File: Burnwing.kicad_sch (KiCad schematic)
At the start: 57 parts, among them J1 Conn_01x04_Socket, J2 USB Type C, J3 Conn_01x02_Pin, J4 Conn_01x02_Pin, J5 Conn_01x06_MountingPin, J6 Conn_01x06_MountingPin, Q1 AONR21307, SW1 SW_DIP_x02, U1 HUSB238, U2 BTS7030-2EPA, U3 TPS70933QDBVRQ1

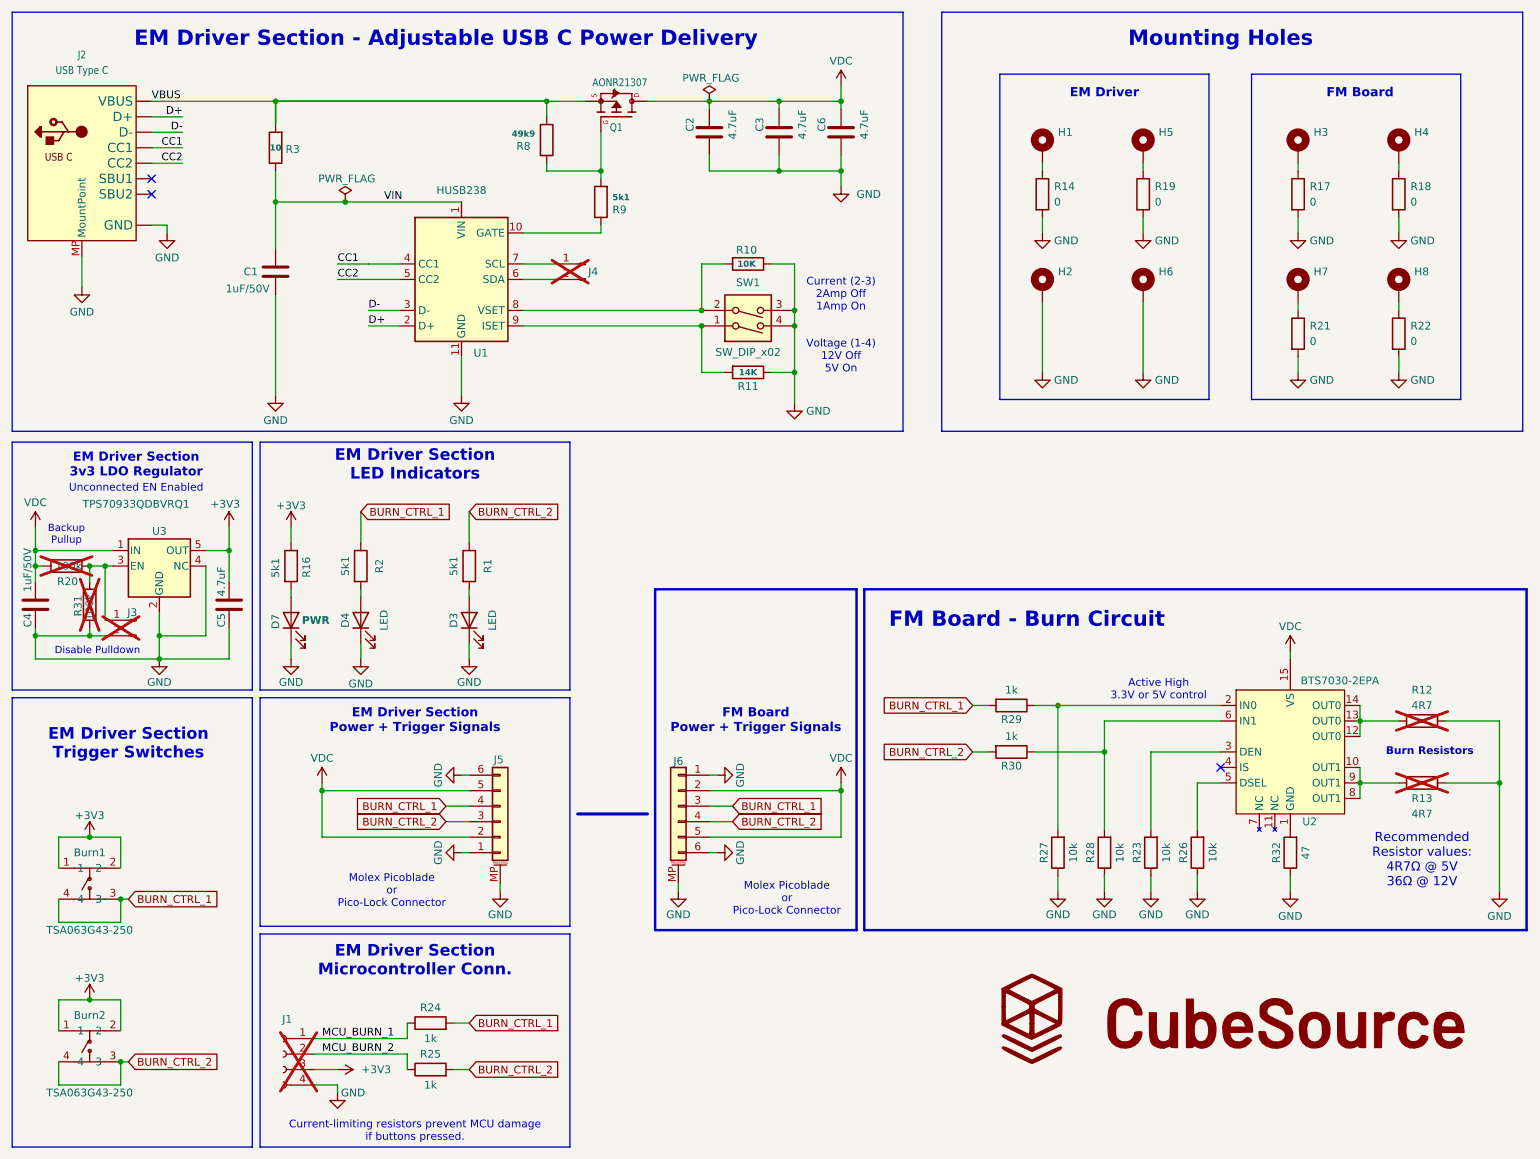
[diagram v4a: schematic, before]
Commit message: Apply design review fixes, clean up BOM and footprint library
Board now passes DRC with 0 violations, 0 unconnected items and 0 schematic
parity errors. ERC is down to one pre-existing power_pin_not_driven on U2 pin 1.

Component values (from the design review):
- R29, R30: 1k -> 3k on the control-line series resistance. At 12 V into a
  3.3 V host this is 25 mW against a 50 mW derated budget; 1k gave 76 mW and
  failed the 50% derate. 3k + the 1k on the J1 path stays under the 4.7k the
  driver datasheet recommends
- R1, R2, R16: 5k1 -> 150R on the LED series resistors. 5k1 gave ~0.25 mA and
  was effectively invisible. 150R gives 8.7 mA at 3.3 V and stays safe at 20 mA
  if a control line is driven at 5 V
- R20, R31: 100k -> 10k on the LDO EN divider pads (both DNP). 100k is high
  enough to affect the LDO's turn-on and settling behaviour if ever populated

Connectivity:
- Wire Burn2 pin 1 to +3V3. Burn1 had both pads 1 and 2 on the net but Burn2
  had only pad 2, leaving pad 1 on no net at all
- Add jumper pad groups (1+2, 3+4) to the tact switch footprint, declaring the
  internally bonded pads so DRC no longer reports them as unconnected. This
  resolved the remaining teardrop unconnected items

BOM correctness:
- C105580 is a 5.1k part but was assigned to five components across three
  values. R9 keeps it; R1/R2/R16 -> C22808 (150R), R11 -> C881028 (14k)
- Burn1, Burn2 and U2 stored their code in a field named "LCSC Part" rather
  than "LCSC", so a BOM export keyed on LCSC silently dropped them, including
  the driver IC
- Add missing codes: R29/R30 -> C881244, R17/R18/R19/R21/R22 -> C100044,
  matching R14

Footprint library:
- Add MountingHole_2.2mm_M2_Pad_4mm and reassign H2/H6 to it. Those two sit
  closest to the panel break line and use a 4.0 mm pad against 4.4 mm on the
  other six; a shared footprint could not represent both
- CONN-SMD_6P-P1.50_A1501WRB-S-6P: convert from the legacy (module format left
  by the EasyEDA importer, which also carried an e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
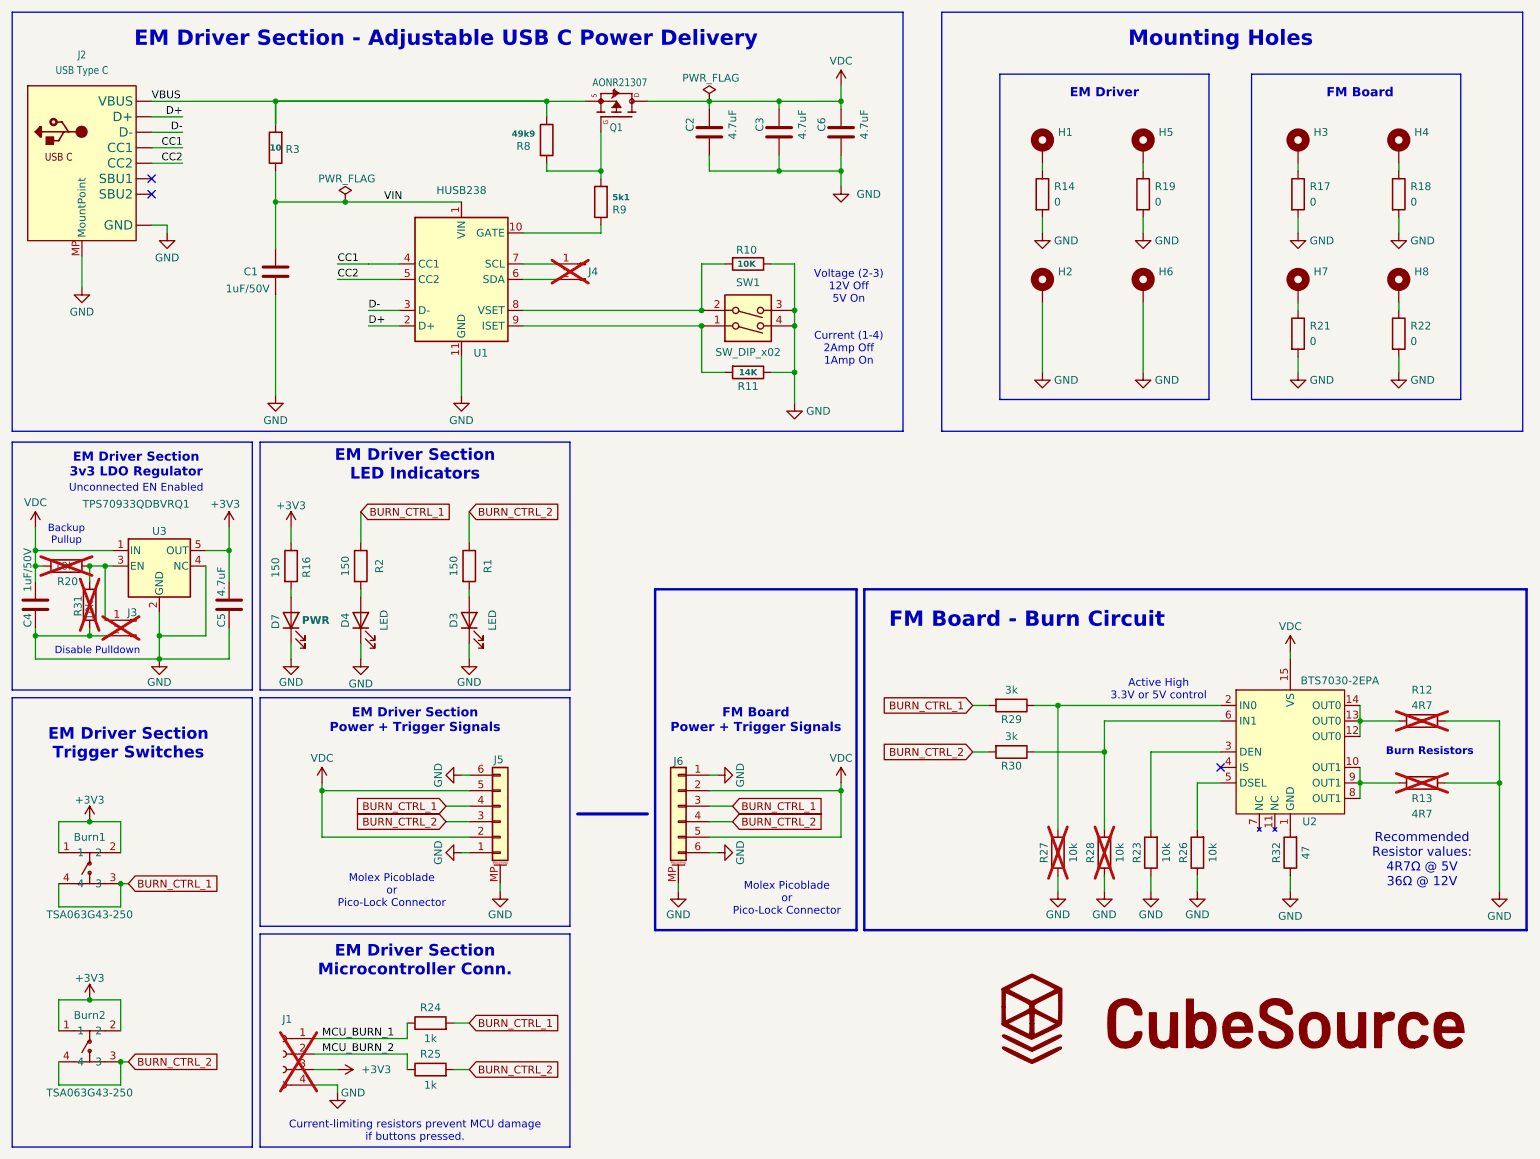
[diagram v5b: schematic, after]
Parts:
- Burn1: symbol Burnwing:TSA063G43-250 -> Burnwing:TSA063G43-250_1; LCSC (none) -> C294564
- Burn2: LCSC (none) -> C294564
- H2, H6: footprint Burnwing:MountingHole_2.2mm_M2_Pad -> Burnwing:MountingHole_2.2mm_M2_Pad_4mm
- J5: footprint Burnwing:Molex_Pico-Lock_and_PicoBlade -> Burnwing:Molex_Pico-Lock_and_PicoBlade_Mirror
- R1, R16, R2: value 5k1 -> 150; LCSC C105580 -> C22808
- R11: LCSC C105580 -> C881028
- R17, R18, R19, R21, R22: LCSC (none) -> C100044
- R20, R31: value 100k -> 10k
- R27, R28: now not fitted; now left out of the parts list
- R29, R30: value 1k -> 3k; LCSC (none) -> C881244
- U2: LCSC (none) -> C534836
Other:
- note added: "Current (1-4) 2Amp Off 1Amp On"
- note added: "Voltage (2-3) 12V Off 5V On"
- note removed: "Current (2-3) 2Amp Off 1Amp On"
- note removed: "Voltage (1-4) 12V Off 5V On"
- moved on the sheet: Burn1

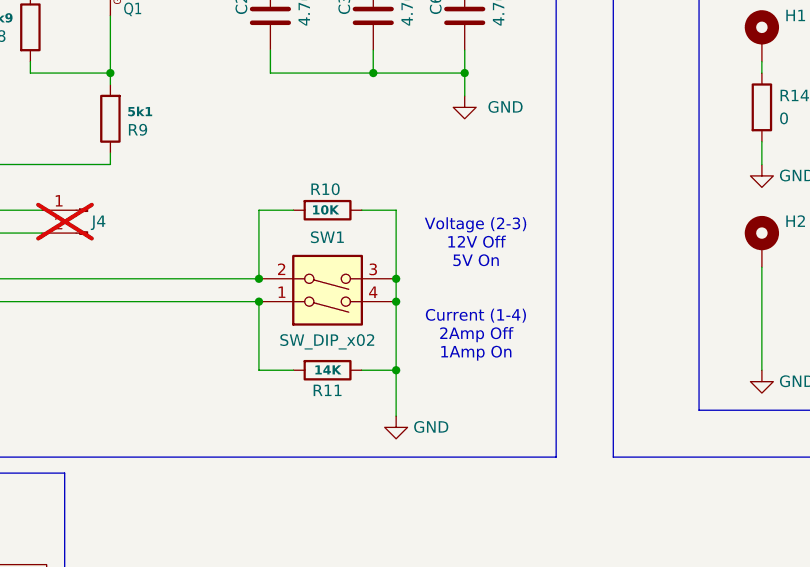
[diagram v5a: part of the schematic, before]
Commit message: Correct SW1 pole assignment so legends match function
The DIP switch poles drove the opposite functions to their printed legends:
the pole marked for voltage switched ISET, and the pole marked for current
switched VSET.

Swap the pole assignments so each matches its legend:
- SW1 pin 1 (switch 1, pins 1-4) now drives VSET
- SW1 pin 2 (switch 2, pins 2-3) now drives ISET

Schematic annotation updated to match: "Voltage (1-4)" and "Current (2-3)",
previously "(2-3)" and "(1-4)" respectively.

Resistor values are unchanged and were always correct - R10 = 10k on VSET
requests 12 V open / 5 V closed, R11 = 14k on ISET requests 2.25 A open /
1.25 A closed. Only the mapping of function to physical actuator changed, so
PD behaviour for a correctly-set switch is identical.

DRC: 0 violations, 0 unconnected, 0 schematic parity errors.
ERC: 1 pre-existing power_pin_not_driven on U2 pin 1.
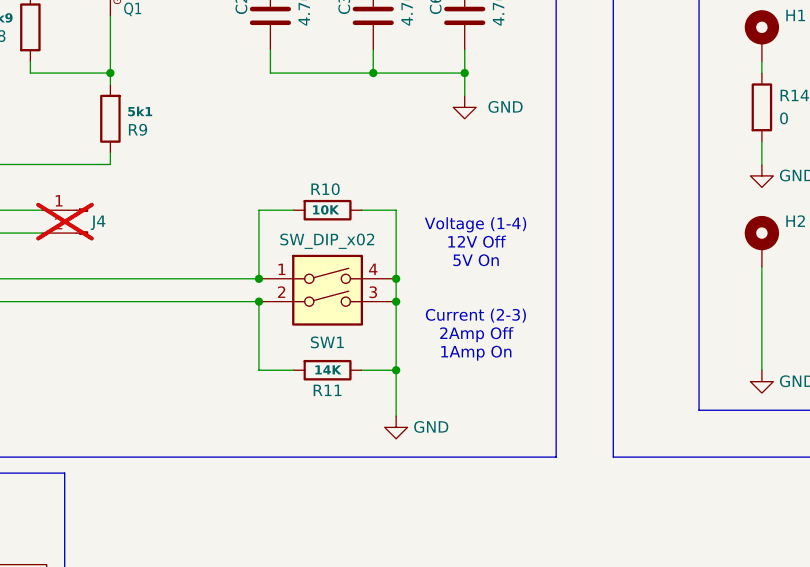
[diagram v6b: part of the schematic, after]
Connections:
- net at R11.2, U1.9 (ISET): now also SW1.2; no longer SW1.1
- net at R10.2, U1.8 (VSET): now also SW1.1; no longer SW1.2
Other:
- note added: "Current (2-3) 2Amp Off 1Amp On"
- note added: "Voltage (1-4) 12V Off 5V On"
- note removed: "Current (1-4) 2Amp Off 1Amp On"
- note removed: "Voltage (2-3) 12V Off 5V On"
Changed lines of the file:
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@@
 		)
 	)
-	(text "Voltage (2-3)\n12V Off\n5V On"
+	(text "Voltage (1-4)\n12V Off\n5V On"
 		(exclude_from_sim no)
 		(at 151.13 59.69 0)
@@
 		)
 	)
-	(text "Current (1-4)\n2Amp Off\n1Amp On"
+	(text "Current (2-3)\n2Amp Off\n1Amp On"
 		(exclude_from_sim no)
 		(at 151.13 69.85 0)
@@
 	)
 	(junction
-		(at 142.24 66.04)
+		(at 127 63.5)
 		(diameter 0)
 		(color 0 0 0 0)
@@
 	)
 	(junction
+		(at 142.24 66.04)
+		(diameter 0)
+		(color 0 0 0 0)
+	)
+	(junction
 		(at 17.78 105.41)
 		(diameter 0)
@@
 	)
 	(junction
+		(at 127 66.04)
+		(diameter 0)
+		(color 0 0 0 0)
+	)
+	(junction
 		(at 26.67 176.53)
 		(diameter 0)
@@
 	)
 	(junction
+		(at 142.24 63.5)
+		(diameter 0)
+		(color 0 0 0 0)
+	)
+	(junction
 		(at 142.24 73.66)
 		(diameter 0)
@@
 	)
 	(junction
-		(at 127 66.04)
-		(diameter 0)
-		(color 0 0 0 0)
-	)
-	(junction
 		(at 17.78 102.87)
 		(diameter 0)
@@
 	)
 	(junction
-		(at 142.24 63.5)
-		(diameter 0)
-		(color 0 0 0 0)
-	)
-	(junction
 		(at 31.75 186.69)
 		(diameter 0)
@@
 	)
 	(junction
-		(at 127 63.5)
-		(diameter 0)
-		(color 0 0 0 0)
-	)
-	(junction
 		(at 68.58 45.72)
 		(diameter 0)
@@
 	(wire
 		(pts
+			(xy 142.24 66.04) (xy 142.24 73.66)
+		)
+		(stroke
+			(width 0)
+			(type default)
+		)
+	)
+	(wire
+		(pts
 			(xy 138.43 55.88) (xy 142.24 55.88)
 		)
@@
 	(wire
 		(pts
-			(xy 57.15 29.21) (xy 101.6 29.21)
+			(xy 142.24 63.5) (xy 142.24 66.04)
 		)
 		(stroke
@@
 	(wire
 		(pts
-			(xy 142.24 63.5) (xy 142.24 66.04)
+			(xy 57.15 29.21) (xy 101.6 29.21)
 		)
 		(stroke
@@
 	(wire
 		(pts
-			(xy 142.24 66.04) (xy 142.24 73.66)
-		)
-		(stroke
-			(width 0)
-			(type default)
-		)
-	)
-	(wire
-		(pts
 			(xy 101.6 29.21) (xy 107.95 29.21)
 		)
@@
 	(symbol
 		(lib_id "Burnwing:SW_DIP_x02")
-		(at 134.62 63.5 0)
-		(mirror x)
+		(at 134.62 66.04 0)
 		(unit 1)
 		(body_style 1)
@@
 		(dnp no)
 		(property "Reference" "SW1"
-			(at 134.62 58.928 0)
+			(at 134.62 70.612 0)
 			(show_name no)
 			(do_not_autoplace no)
@@
 		)
 		(property "Value" "SW_DIP_x02"
-			(at 134.62 70.358 0)
+			(at 134.62 59.182 0)
 			(show_name no)
 			(do_not_autoplace no)
@@
 		)
 		(property "Footprint" "Burnwing:2_Dipswitch"
-			(at 134.62 63.5 0)
+			(at 134.62 66.04 0)
 			(hide yes)
 			(show_name no)
@@
 		)
 		(property "Datasheet" ""
-			(at 134.62 63.5 0)
+			(at 134.62 66.04 0)
 			(hide yes)
 			(show_name no)
@@
 		)
 		(property "Description" "2x DIP Switch, Single Pole Single Throw (SPST) switch, small symbol"
-			(at 134.62 63.5 0)
+			(at 134.62 66.04 0)
 			(hide yes)
 			(show_name no)

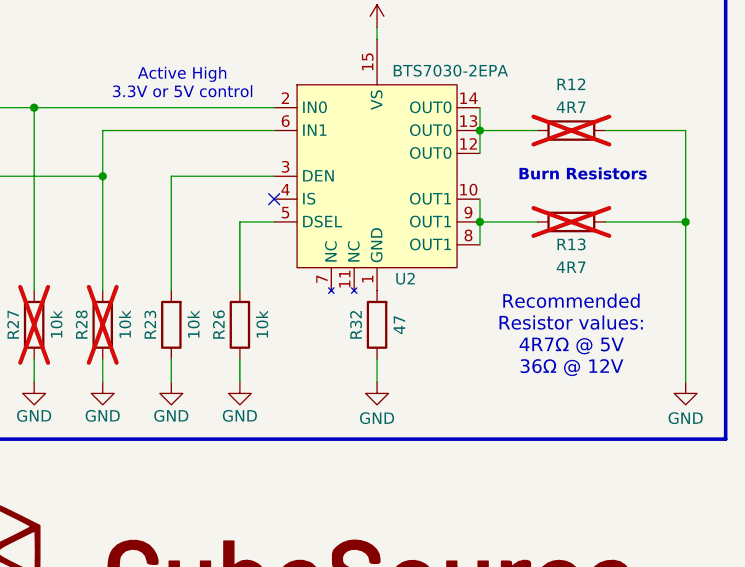
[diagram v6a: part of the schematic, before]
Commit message: Docs updates
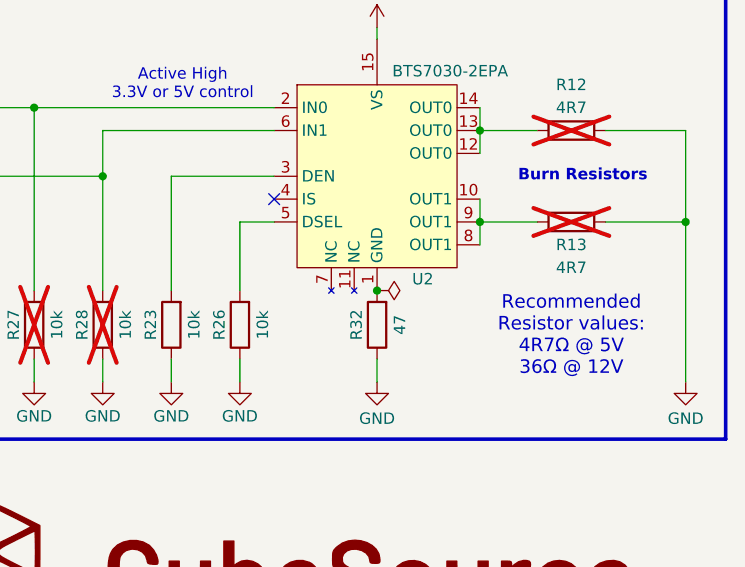
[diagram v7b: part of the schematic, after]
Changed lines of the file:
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@@
 	)
 	(junction
+		(at 223.52 148.59)
+		(diameter 0)
+		(color 0 0 0 0)
+	)
+	(junction
 		(at 127 66.04)
 		(diameter 0)
@@
 			)
 		)
-		(property "Datasheet" "https://www.ti.com/lit/ds/symlink/tps709.pdf"
+		(property "Datasheet" "https://www.ti.com/lit/ds/symlink/tlv709.pdf?ts=1786928765631"
 			(at 38.1 127 0)
 			(hide yes)
@@
 	)
 	(symbol
+		(lib_id "power:PWR_FLAG")
+		(at 223.52 148.59 270)
+		(unit 1)
+		(body_style 1)
+		(exclude_from_sim no)
+		(in_bom yes)
+		(on_board yes)
+		(in_pos_files yes)
+		(dnp no)
+		(property "Reference" "#FLG03"
+			(at 225.425 148.59 0)
+			(hide yes)
+			(show_name no)
+			(do_not_autoplace no)
+			(effects
+				(font
+					(size 1.27 1.27)
+				)
+			)
+		)
+		(property "Value" "PWR_FLAG"
+			(at 227.33 148.844 0)
+			(hide yes)
+			(show_name no)
+			(do_not_autoplace no)
+			(effects
+				(font
+					(size 1.27 1.27)
+				)
+			)
+		)
+		(property "Footprint" ""
+			(at 223.52 148.59 0)
+			(hide yes)
+			(show_name no)
+			(do_not_autoplace no)
+			(effects
+				(font
+					(size 1.27 1.27)
+				)
+			)
+		)
+		(property "Datasheet" ""
+			(at 223.52 148.59 0)
+			(hide yes)
+			(show_name no)
+			(do_not_autoplace no)
+			(effects
+				(font
+					(size 1.27 1.27)
+				)
+			)
+		)
+		(property "Description" "Special symbol for telling ERC where power comes from"
+			(at 223.52 148.59 0)
+			(hide yes)
+			(show_name no)
+			(do_not_autoplace no)
+			(effects
+				(font
+					(size 1.27 1.27)
+				)
+			)
+		)
+		(pin "1"
+		)
+		(instances
+			(project "Burnwing"
+				(path "/668c3a07-3236-4b27-b3a6-03c249258f7f"
+					(reference "#FLG03")
+					(unit 1)
+				)
+			)
+		)
+	)
+	(symbol
 		(lib_id "power:GND")
 		(at 182.88 50.8 0)
@@
 		(dnp no)
 		(property "Reference" "U2"
-			(at 226.695 147.32 0)
+			(at 228.6 147.32 0)
 			(show_name no)
 			(do_not_autoplace no)
@@
 		(body_style 1)
 		(exclude_from_sim no)
-		(in_bom yes)
-		(on_board yes)
-		(in_pos_files yes)
+		(in_bom no)
+		(on_board no)
+		(in_pos_files no)
 		(dnp no)
 		(fields_autoplaced yes)
@@
 			)
 		)
-		(property "Datasheet" "https://cdn-learn.adafruit.com/assets/assets/000/125/150/original/husb238_datasheet_full.pdf"
+		(property "Datasheet" "https://en.hynetek.com/uploadfiles/site/219/news/b038530d-67c0-4ba0-9269-de0e666cb35b.pdf"
 			(at 87.63 58.42 0)
 			(hide yes)
